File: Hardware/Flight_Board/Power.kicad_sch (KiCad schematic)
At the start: 0 parts

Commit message: Created power schematic
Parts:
- added C1: 10u, symbol Device:C
- added C2, C24: 22u, symbol Device:C
- added C5: 47p, symbol Device:C
- added C6: 330n, symbol Device:C
- added L1: 3.3u, symbol Device:L
- added R1: 31.6k, symbol Device:R
- added R2: 10k, symbol Device:R
- added TP1: TP1, symbol Connector:TestPoint
- added U9: ~, Package_SO:TSOP-6_1.65x3.05mm_P0.95mm, symbol Project:AP62200WU-7
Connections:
- new net: C5.2, R1.2, R2.1, U9.4 (FB)
- new net: C2.1, C24.2
- new net: C6.1, L1.1, U9.2 (SW)
- new net: TP1.1, U9.5 (EN)
- new net: C6.2, U9.6 (BST)
- new net GND: C1.2, C2.2, R2.2, U9.1 (GND)
- new net Vin: C1.1, U9.3 (VIN)
- new net Vout: C24.1, C5.1, L1.2, R1.1

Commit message: clean up and finalize initial design
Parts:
- U7: renamed from U9; value ~ -> AP62200WU
- renumbered C1 to C20, C6 to C21, C5 to C22, C24 to C23, C2 to C24, R1 to R6, R2 to R7, TP1 to TP2
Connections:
- net GND: now also C23.2
- net Vout: now also C24.1
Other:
- moved on the sheet: C24

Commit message: Added Mason's Feedback
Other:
- note added: "R6 = 31.6kOhms R7 = 10kOhms"
- note added: "R6 = R7*(Vout/Vfb - 1)"
- note added: "Via DataSheet"
- note added: "Vout = 3.3V"
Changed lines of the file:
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@@
     (stroke (width 0) (type default))
+  )
+  (text "R6 = 31.6kOhms\nR7 = 10kOhms" (at 212.09 74.93 0)
+    (effects (font (size 1.27 1.27)) (justify left bottom))
+  )
+  (text "Vout = 3.3V\n" (at 212.09 69.85 0)
+    (effects (font (size 1.27 1.27)) (justify left bottom))
+  )
+  (text "R6 = R7*(Vout/Vfb - 1)" (at 212.09 67.31 0)
+    (effects (font (size 1.27 1.27)) (justify left bottom))
+  )
+  (text "Via DataSheet\n" (at 229.87 73.66 0)
+    (effects (font (size 1.27 1.27)) (justify left bottom))
   )
   (hierarchical_label "Vout" (shape output) (at 198.12 72.39 0) (fields_autoplaced)

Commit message: Clean up, relabel all refdes, and add autosaved files to gitignore
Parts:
- renumbered R6 to R8, R7 to R9
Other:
- note added: "R8 = 31.6kOhms R9 = 10kOhms"
- note added: "R8 = R9*(Vout/Vfb - 1)"
- note removed: "R6 = 31.6kOhms R7 = 10kOhms"
- note removed: "R6 = R7*(Vout/Vfb - 1)"

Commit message: Add LEDs and test points
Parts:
- added D1: POWER, symbol Device:LED
- added R26: 22k, symbol Device:R
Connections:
- net GND: now also D1.1 (K)
- net Vout: now also R26.1
- net Vin renamed VBat
- new net: D1.2 (A), R26.2
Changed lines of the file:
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@@
   (junction (at 148.59 72.39) (diameter 0) (color 0 0 0 0)
   )
+  (junction (at 223.52 72.39) (diameter 0) (color 0 0 0 0)
+  )
   (wire (pts (xy 184.15 72.39) (xy 195.58 72.39))
     (stroke (width 0) (type default))
@@
     (stroke (width 0) (type default))
   )
-  (wire (pts (xy 195.58 72.39) (xy 198.12 72.39))
+  (wire (pts (xy 195.58 72.39) (xy 223.52 72.39))
     (stroke (width 0) (type default))
   )
@@
     (stroke (width 0) (type default))
   )
+  (wire (pts (xy 223.52 72.39) (xy 223.52 78.74))
+    (stroke (width 0) (type default))
+  )
   (wire (pts (xy 139.7 85.09) (xy 148.59 85.09))
     (stroke (width 0) (type default))
@@
     (stroke (width 0) (type default))
   )
+  (wire (pts (xy 223.52 72.39) (xy 236.22 72.39))
+    (stroke (width 0) (type default))
+  )
   (wire (pts (xy 148.59 72.39) (xy 151.13 72.39))
     (stroke (width 0) (type default))
@@
     (stroke (width 0) (type default))
   )
-  (text "R8 = 31.6kOhms\nR9 = 10kOhms" (at 212.09 74.93 0)
+  (text "R8 = 31.6kOhms\nR9 = 10kOhms" (at 182.88 120.65 0)
     (effects (font (size 1.27 1.27)) (justify left bottom))
   )
-  (text "Vout = 3.3V\n" (at 212.09 69.85 0)
+  (text "Vout = 3.3V\n" (at 182.88 115.57 0)
     (effects (font (size 1.27 1.27)) (justify left bottom))
   )
-  (text "R8 = R9*(Vout/Vfb - 1)" (at 212.09 67.31 0)
+  (text "R8 = R9*(Vout/Vfb - 1)" (at 182.88 113.03 0)
     (effects (font (size 1.27 1.27)) (justify left bottom))
   )
-  (text "Via DataSheet\n" (at 229.87 74.93 0)
+  (text "Via DataSheet\n" (at 200.66 120.65 0)
     (effects (font (size 1.27 1.27)) (justify left bottom))
   )
-  (hierarchical_label "Vout" (shape output) (at 198.12 72.39 0) (fields_autoplaced)
+  (hierarchical_label "Vout" (shape output) (at 236.22 72.39 0) (fields_autoplaced)
     (effects (font (size 1.27 1.27)) (justify left))
   )
-  (hierarchical_label "Vin" (shape input) (at 101.6 82.55 180) (fields_autoplaced)
+  (hierarchical_label "VBat" (shape input) (at 101.6 82.55 180) (fields_autoplaced)
     (effects (font (size 1.27 1.27)) (justify right))
+  )
+  (symbol (lib_id "power:GND") (at 223.52 93.98 0) (unit 1)
+    (in_bom yes) (on_board yes) (dnp no) (fields_autoplaced)
+    (property "Reference" "#PWR063" (at 223.52 100.33 0)
+      (effects (font (size 1.27 1.27)) hide)
+    )
+    (property "Value" "GND" (at 223.52 99.06 0)
+      (effects (font (size 1.27 1.27)))
+    )
+    (property "Footprint" "" (at 223.52 93.98 0)
+      (effects (font (size 1.27 1.27)) hide)
+    )
+    (property "Datasheet" "" (at 223.52 93.98 0)
+      (effects (font (size 1.27 1.27)) hide)
+    )
+    (pin "1")
+    (instances
+      (project "Flight_Board"
+        (path "/e8eb85d5-f1ff-4500-895d-25b9ff5f6d36/7c06db2a-34f5-45c0-9668-fbbbd940678c"
+          (reference "#PWR063") (unit 1)
+        )
+        (path "/e8eb85d5-f1ff-4500-895d-25b9ff5f6d36/bc23ea56-d50e-4ce7-856f-e38dfbe72971"
+          (reference "#PWR073") (unit 1)
+        )
+      )
+    )
   )
   (symbol (lib_id "Device:R") (at 172.72 78.74 0) (unit 1)
@@
     )
   )
+  (symbol (lib_id "Device:LED") (at 223.52 90.17 90) (unit 1)
+    (in_bom yes) (on_board yes) (dnp no) (fields_autoplaced)
+    (property "Reference" "D1" (at 227.33 90.4875 90)
+      (effects (font (size 1.27 1.27)) (justify right))
+    )
+    (property "Value" "POWER" (at 227.33 93.0275 90)
+      (effects (font (size 1.27 1.27)) (justify right))
+    )
+    (property "Footprint" "" (at 223.52 90.17 0)
+      (effects (font (size 1.27 1.27)) hide)
+    )
+    (property "Datasheet" "~" (at 223.52 90.17 0)
+      (effects (font (size 1.27 1.27)) hide)
+    )
+    (pin "1")
+    (pin "2")
+    (instances
+      (project "Flight_Board"
+        (path "/e8eb85d5-f1ff-4500-895d-25b9ff5f6d36/7c06db2a-34f5-45c0-9668-fbbbd940678c"
+          (reference "D1") (unit 1)
+        )
+        (path "/e8eb85d5-f1ff-4500-895d-25b9ff5f6d36/bc23ea56-d50e-4ce7-856f-e38dfbe72971"
+          (reference "D3") (unit 1)
+        )
+      )
+    )
+  )
   (symbol (lib_id "Device:L") (at 154.94 72.39 90) (unit 1)
     (in_bom yes) (on_board yes) (dnp no) (fields_autoplaced)
@@
         )
       )
+    )
+  )
+  (symbol (lib_id "Device:R") (at 223.52 82.55 0) (unit 1)
+    (in_bom yes) (on_board yes) (dnp no) (fields_autoplaced)
+    (property "Reference" "R26" (at 226.06 81.28 0)
+      (effects (font (size 1.27 1.27)) (justify left))
+    )
+    (property "Value" "22k" (at 226.06 83.82 0)
+      (effects (font (size 1.27 1.27)) (justify left))
+    )
+    (property "Footprint" "" (at 221.742 82.55 90)
+      (effects (font (size 1.27 1.27)) hide)
+    )
+    (property "Datasheet" "~" (at 223.52 82.55 0)
+      (effects (font (size 1.27 1.27)) hide)
+    )
+    (pin "1")
+    (pin "2")
+    (instances
+      (project "Flight_Board"
+        (path "/e8eb85d5-f1ff-4500-895d-25b9ff5f6d36/7c06db2a-34f5-45c0-9668-fbbbd940678c"
+          (reference "R26") (unit 1)
+        )
+        (path "/e8eb85d5-f1ff-4500-895d-25b9ff5f6d36/bc23ea56-d50e-4ce7-856f-e38dfbe72971"
+          (reference "R36") (unit 1)
+        )
+      )

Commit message: final touches, bom, footprints
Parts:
- added TP1: 3V3, TestPoint:TestPoint_THTPad_2.0x2.0mm_Drill1.0mm, symbol Connector:TestPoint
- C20, C21, C22, C23, C24: footprint (none) -> Capacitor_SMD:C_0603_1608Metric_Pad1.08x0.95mm_HandSolder
- D1: footprint (none) -> LED_SMD:LED_0603_1608Metric_Pad1.05x0.95mm_HandSolder
- L1: value 3.3u -> 4.7u; footprint (none) -> Inductor_SMD:L_Taiyo-Yuden_NR-60xx_HandSoldering
- R26, R8, R9: footprint (none) -> Resistor_SMD:R_0603_1608Metric_Pad0.98x0.95mm_HandSolder
- TP2: value TP1 -> EN; footprint (none) -> TestPoint:TestPoint_Pad_D1.0mm
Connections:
- net Vout: now also TP1.1
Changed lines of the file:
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@@
       (effects (font (size 1.27 1.27)) (justify left))
     )
-    (property "Footprint" "" (at 170.942 78.74 90)
+    (property "Footprint" "Resistor_SMD:R_0603_1608Metric_Pad0.98x0.95mm_HandSolder" (at 170.942 78.74 90)
       (effects (font (size 1.27 1.27)) hide)
     )
@@
       (effects (font (size 1.27 1.27)) (justify left))
     )
-    (property "Footprint" "" (at 107.6452 97.79 0)
+    (property "Footprint" "Capacitor_SMD:C_0603_1608Metric_Pad1.08x0.95mm_HandSolder" (at 107.6452 97.79 0)
       (effects (font (size 1.27 1.27)) hide)
     )
@@
       (effects (font (size 1.27 1.27)) (justify left))
     )
-    (property "Footprint" "" (at 196.5452 82.55 0)
+    (property "Footprint" "Capacitor_SMD:C_0603_1608Metric_Pad1.08x0.95mm_HandSolder" (at 196.5452 82.55 0)
       (effects (font (size 1.27 1.27)) hide)
     )
@@
       (effects (font (size 1.27 1.27)) (justify left))
     )
-    (property "Footprint" "" (at 162.2552 82.55 0)
+    (property "Footprint" "Capacitor_SMD:C_0603_1608Metric_Pad1.08x0.95mm_HandSolder" (at 162.2552 82.55 0)
       (effects (font (size 1.27 1.27)) hide)
     )
@@
       (effects (font (size 1.27 1.27)) (justify right))
     )
-    (property "Footprint" "" (at 223.52 90.17 0)
+    (property "Footprint" "LED_SMD:LED_0603_1608Metric_Pad1.05x0.95mm_HandSolder" (at 223.52 90.17 0)
       (effects (font (size 1.27 1.27)) hide)
     )
@@
       (effects (font (size 1.27 1.27)))
     )
-    (property "Value" "3.3u" (at 154.94 69.85 90)
-      (effects (font (size 1.27 1.27)))
-    )
-    (property "Footprint" "" (at 154.94 72.39 0)
+    (property "Value" "4.7u" (at 154.94 69.85 90)
+      (effects (font (size 1.27 1.27)))
+    )
+    (property "Footprint" "Inductor_SMD:L_Taiyo-Yuden_NR-60xx_HandSoldering" (at 154.94 72.39 0)
       (effects (font (size 1.27 1.27)) hide)
     )
@@
         (path "/e8eb85d5-f1ff-4500-895d-25b9ff5f6d36/bc23ea56-d50e-4ce7-856f-e38dfbe72971"
           (reference "L1") (unit 1)
+        )
+      )
+    )
+  )
+  (symbol (lib_id "Connector:TestPoint") (at 223.52 72.39 0) (unit 1)
+    (in_bom yes) (on_board yes) (dnp no)
+    (property "Reference" "TP1" (at 222.25 67.31 90)
+      (effects (font (size 1.27 1.27)) (justify left) hide)
+    )
+    (property "Value" "3V3" (at 224.79 68.58 0)
+      (effects (font (size 1.27 1.27)) (justify left))
+    )
+    (property "Footprint" "TestPoint:TestPoint_THTPad_2.0x2.0mm_Drill1.0mm" (at 228.6 72.39 0)
+      (effects (font (size 1.27 1.27)) hide)
+    )
+    (property "Datasheet" "~" (at 228.6 72.39 0)
+      (effects (font (size 1.27 1.27)) hide)
+    )
+    (pin "1")
+    (instances
+      (project "Flight_Board"
+        (path "/e8eb85d5-f1ff-4500-895d-25b9ff5f6d36/52cae81a-54fe-42c0-9a19-be88b271d004"
+          (reference "TP1") (unit 1)
+        )
+        (path "/e8eb85d5-f1ff-4500-895d-25b9ff5f6d36"
+          (reference "TP21") (unit 1)
+        )
+        (path "/e8eb85d5-f1ff-4500-895d-25b9ff5f6d36/bc23ea56-d50e-4ce7-856f-e38dfbe72971"
+          (reference "TP22") (unit 1)
         )
       )
@@
       (effects (font (size 1.27 1.27)) (justify left))
     )
-    (property "Footprint" "" (at 149.5552 82.55 0)
+    (property "Footprint" "Capacitor_SMD:C_0603_1608Metric_Pad1.08x0.95mm_HandSolder" (at 149.5552 82.55 0)
       (effects (font (size 1.27 1.27)) hide)
     )
@@
       (effects (font (size 1.27 1.27)) (justify left))
     )
-    (property "Footprint" "" (at 185.1152 82.55 0)
+    (property "Footprint" "Capacitor_SMD:C_0603_1608Metric_Pad1.08x0.95mm_HandSolder" (at 185.1152 82.55 0)
       (effects (font (size 1.27 1.27)) hide)
     )
@@
       (effects (font (size 1.27 1.27)) hide)
     )
-    (property "Value" "TP1" (at 113.538 85.09 90)
-      (effects (font (size 1.27 1.27)))
-    )
-    (property "Footprint" "" (at 116.84 82.55 0)
+    (property "Value" "EN" (at 113.538 85.09 90)
+      (effects (font (size 1.27 1.27)))
+    )
+    (property "Footprint" "TestPoint:TestPoint_Pad_D1.0mm" (at 116.84 82.55 0)
       (effects (font (size 1.27 1.27)) hide)
     )
@@
       (effects (font (size 1.27 1.27)) (justify left))
     )
-    (property "Footprint" "" (at 221.742 82.55 90)
+    (property "Footprint" "Resistor_SMD:R_0603_1608Metric_Pad0.98x0.95mm_HandSolder" (at 221.742 82.55 90)
       (effects (font (size 1.27 1.27)) hide)
     )
@@
       (effects (font (size 1.27 1.27)) (justify left))
     )
-    (property "Footprint" "" (at 170.942 93.98 90)
-      (effects (font (size 1.27 1.27)) hide)
-    )
+    (property "Footprint" "Resistor_SMD:R_0603_1608Metric_Pad0.98x0.95mm_HandSolder" (at 170.942 93.98 90)
+      (effects (font (size 1.27 1.27)) hide)
+    )

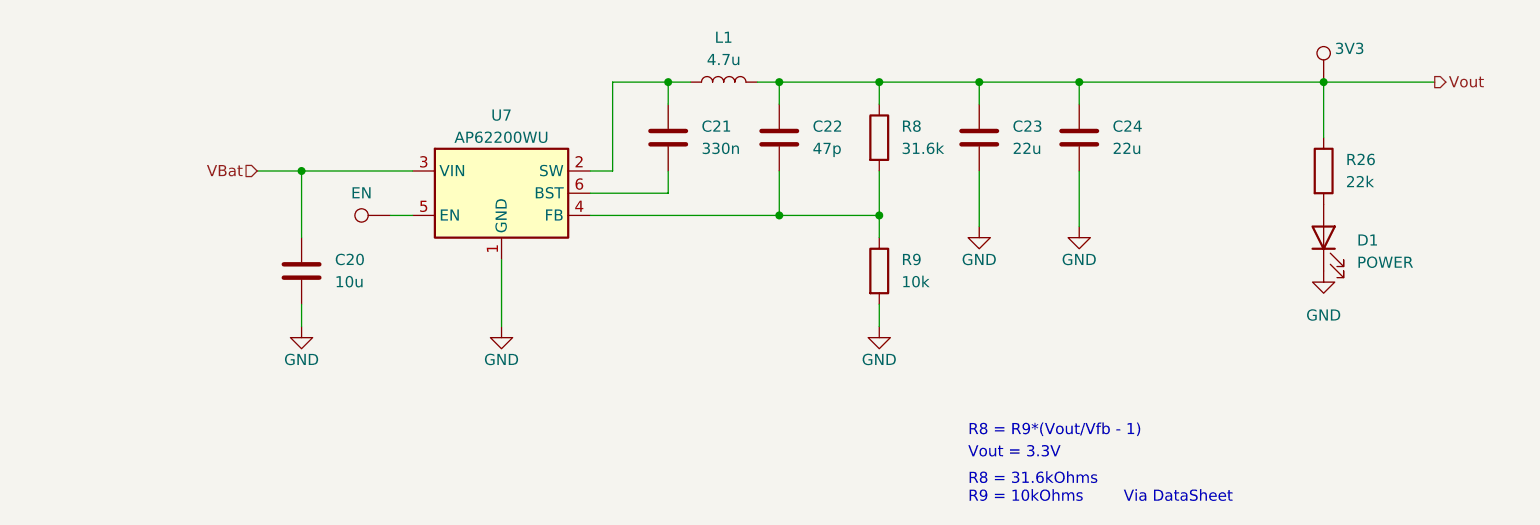
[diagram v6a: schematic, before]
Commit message: begin 4 layer board
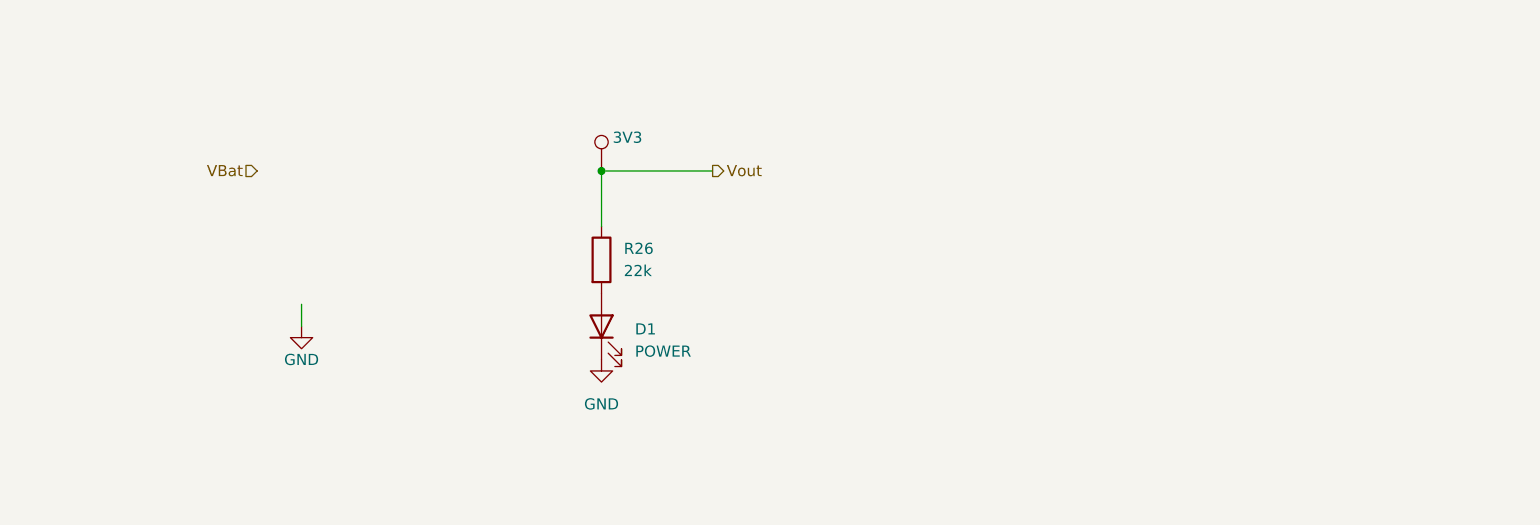
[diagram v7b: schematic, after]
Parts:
- removed C20: 10u, Capacitor_SMD:C_0603_1608Metric_Pad1.08x0.95mm_HandSolder, symbol Device:C
- removed C21: 330n, Capacitor_SMD:C_0603_1608Metric_Pad1.08x0.95mm_HandSolder, symbol Device:C
- removed C22: 47p, Capacitor_SMD:C_0603_1608Metric_Pad1.08x0.95mm_HandSolder, symbol Device:C
- removed C23, C24: 22u, Capacitor_SMD:C_0603_1608Metric_Pad1.08x0.95mm_HandSolder, symbol Device:C
- removed L1: 4.7u, Inductor_SMD:L_Taiyo-Yuden_NR-60xx_HandSoldering, symbol Device:L
- removed R8: 31.6k, Resistor_SMD:R_0603_1608Metric_Pad0.98x0.95mm_HandSolder, symbol Device:R
- removed R9: 10k, Resistor_SMD:R_0603_1608Metric_Pad0.98x0.95mm_HandSolder, symbol Device:R
- removed TP2: EN, TestPoint:TestPoint_Pad_D1.0mm, symbol Connector:TestPoint
- removed U7: AP62200WU, Package_SO:TSOP-6_1.65x3.05mm_P0.95mm, symbol Project:AP62200WU-7
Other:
- note removed: "R8 = 31.6kOhms R9 = 10kOhms"
- note removed: "R8 = R9*(Vout/Vfb - 1)"
- note removed: "Via DataSheet"
- note removed: "Vout = 3.3V"
- moved on the sheet: D1, R26
